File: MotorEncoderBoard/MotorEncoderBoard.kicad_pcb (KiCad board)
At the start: 2 copper layers, 24.3 x 31.8 mm, 13 parts, among them P1 PWR, P2 Out, U1 RPI-579N1, U2 LM311N

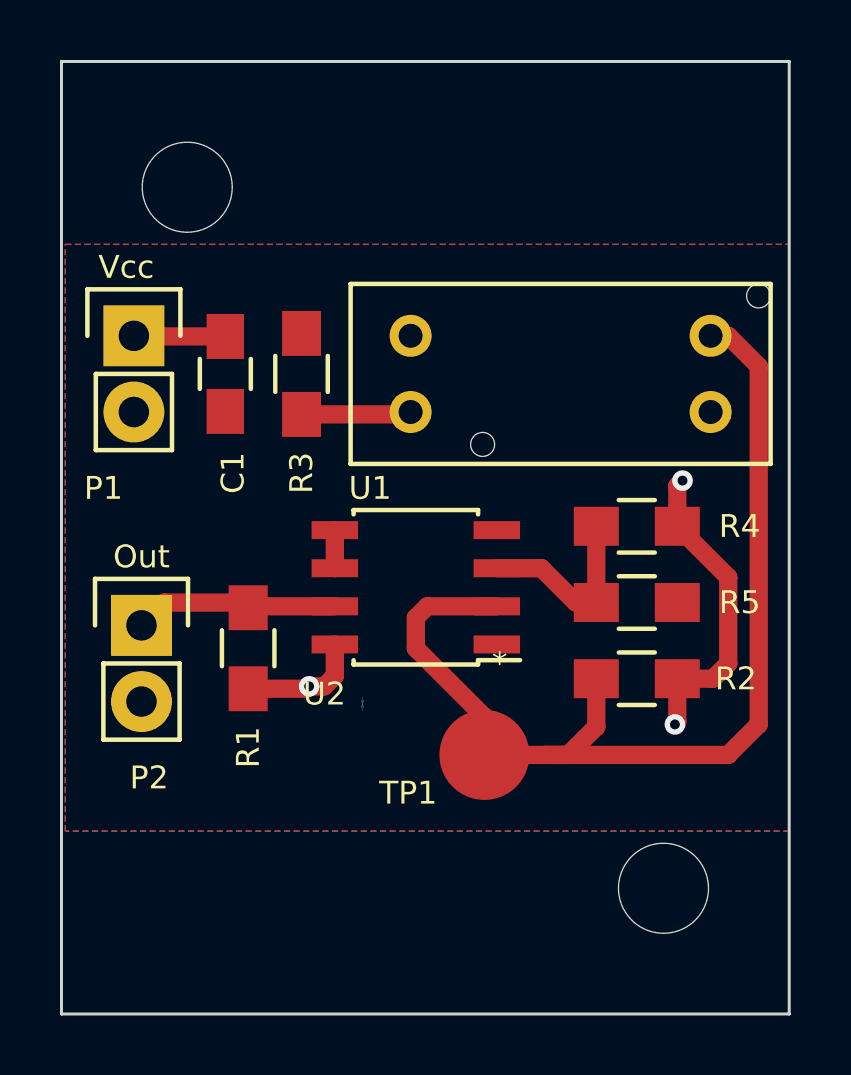
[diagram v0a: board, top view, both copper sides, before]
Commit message: Correction to the motor encoder board
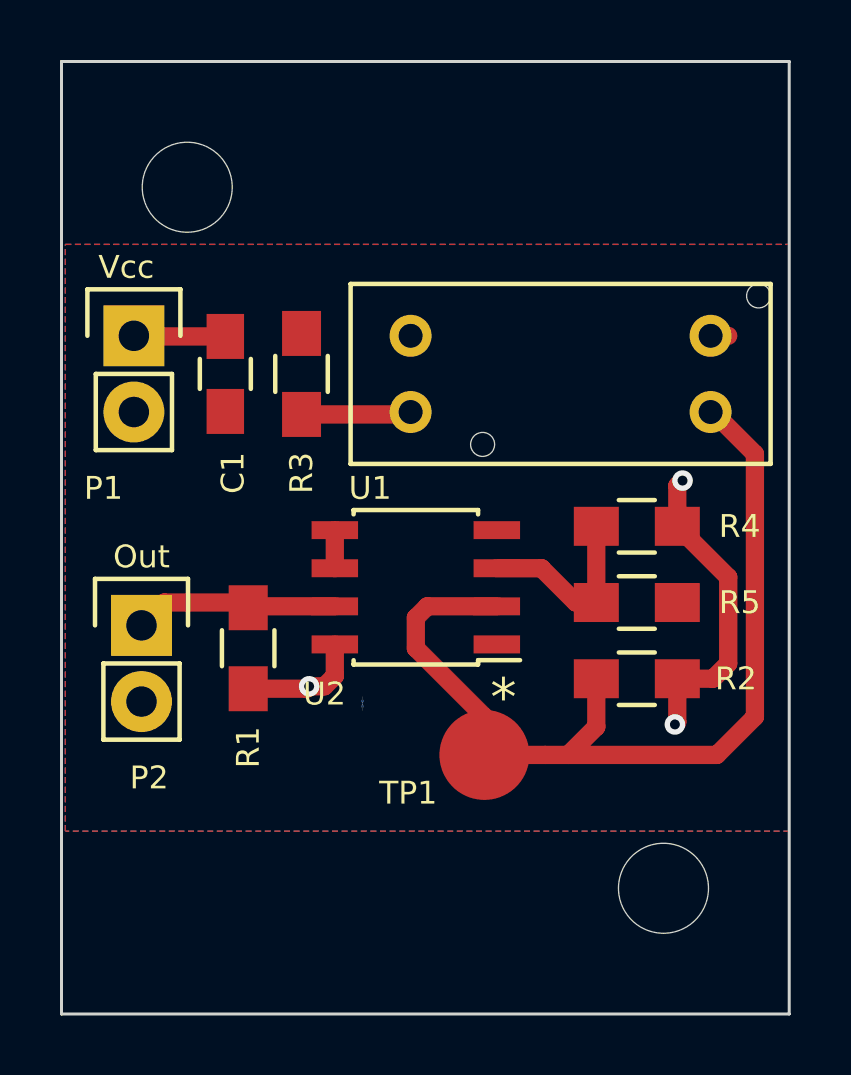
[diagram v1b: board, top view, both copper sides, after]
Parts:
- C1: value C -> 10u
- U2: value LM311N -> LM311D
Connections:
- U1 pad 3: GND -> /OptoOut
- U1 pad 4: /OptoOut -> GND
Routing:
- net /OptoOut: track 35.9 -> 31.7 mm
- net GND: track 0.00 -> 0.92 mm
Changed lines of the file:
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@@
-(kicad_pcb (version 4) (host pcbnew 0.201506222247+5806~23~ubuntu14.04.1-product)
+(kicad_pcb (version 4) (host pcbnew no-vcs-found-product)
   (general
     (links 22)
     (no_connects 0)
-    (area 144.971679 75.34104 176.206241 111.40216)
+    (area 148.412999 77.165999 172.770001 109.016001)
     (thickness 1.6)
     (drawings 16)
-    (tracks 44)
+    (tracks 45)
     (zones 0)
     (modules 13)
@@
       (effects (font (size 0.762 0.762) (thickness 0.127)))
     )
-    (fp_text value C (at 0 2.1 270) (layer F.Fab)
+    (fp_text value 10u (at 0 2.1 270) (layer F.Fab)
       (effects (font (size 0.762 0.762) (thickness 0.127)))
     )
@@
     (pad "" np_thru_hole circle (at 2.6 -2.35 180) (size 0.8 0.8) (drill 0.8) (layers *.Cu *.Mask F.SilkS))
     (pad 3 thru_hole circle (at -5 -1.27 180) (size 1.4 1.4) (drill 0.8) (layers *.Cu *.Mask F.SilkS)
-      (net 2 GND))
+      (net 4 /OptoOut))
     (pad 4 thru_hole circle (at -5 1.27 180) (size 1.4 1.4) (drill 0.8) (layers *.Cu *.Mask F.SilkS)
-      (net 4 /OptoOut))
+      (net 2 GND))
     (pad 2 thru_hole circle (at 5 -1.27 180) (size 1.4 1.4) (drill 0.8) (layers *.Cu *.Mask F.SilkS)
       (net 5 "Net-(R3-Pad1)"))
@@
       (effects (font (size 0.762 0.762) (thickness 0.127)))
     )
-    (fp_text value LM311N (at 0 3.5 180) (layer F.Fab)
+    (fp_text value LM311D (at 0 3.5 180) (layer F.Fab)
       (effects (font (size 0.762 0.762) (thickness 0.127)))
     )
@@
     (effects (font (size 0.762 0.762) (thickness 0.127)))
   )
-  (gr_text * (at 163.068 97.282) (layer F.SilkS)
-    (effects (font (size 0.762 0.762) (thickness 0.127)) (justify mirror))
+  (gr_text * (at 163.195 98.425) (layer F.SilkS)
+    (effects (font (size 1.27 1.27) (thickness 0.127)) (justify mirror))
   )
   (gr_text * (at 158.496 98.806) (layer B.Cu)
@@
   (segment (start 157.574 97.696) (end 157.574 96.647) (width 0.6096) (layer F.Cu) (net 1))
   (segment (start 157.226 98.044) (end 157.574 97.696) (width 0.6096) (layer F.Cu) (net 1))
+  (segment (start 170.1 86.36) (end 170.688 86.36) (width 0.6096) (layer F.Cu) (net 2))
+  (segment (start 170.1 86.36) (end 170.434 86.36) (width 0.6096) (layer F.Cu) (net 2))
   (segment (start 157.574 95.377) (end 154.733 95.377) (width 0.6096) (layer F.Cu) (net 3))
   (segment (start 154.733 95.377) (end 154.606 95.25) (width 0.6096) (layer F.Cu) (net 3))
   (segment (start 154.606 95.25) (end 151.892 95.25) (width 0.6096) (layer F.Cu) (net 3))
   (segment (start 151.892 95.25) (end 151.13 96.012) (width 0.6096) (layer F.Cu) (net 3))
-  (segment (start 170.1 86.36) (end 170.688 86.36) (width 0.6096) (layer F.Cu) (net 4))
-  (segment (start 170.688 86.36) (end 171.704 87.376) (width 0.6096) (layer F.Cu) (net 4))
-  (segment (start 170.688 100.33) (end 164.592 100.33) (width 0.6096) (layer F.Cu) (net 4))
-  (segment (start 171.704 99.314) (end 170.688 100.33) (width 0.6096) (layer F.Cu) (net 4))
-  (segment (start 171.704 87.376) (end 171.704 99.314) (width 0.6096) (layer F.Cu) (net 4))
-  (segment (start 170.1 86.36) (end 170.434 86.36) (width 0.6096) (layer F.Cu) (net 4))
+  (segment (start 170.1 88.9) (end 170.18 88.9) (width 0.6096) (layer F.Cu) (net 4) (status C00000))
+  (segment (start 170.18 88.9) (end 171.577 90.297) (width 0.6096) (layer F.Cu) (net 4) (status 400000))
+  (segment (start 171.577 90.297) (end 171.577 99.06) (width 0.6096) (layer F.Cu) (net 4))
+  (segment (start 171.577 99.06) (end 170.307 100.33) (width 0.6096) (layer F.Cu) (net 4))
+  (segment (start 170.307 100.33) (end 165.354 100.33) (width 0.6096) (layer F.Cu) (net 4))
   (segment (start 162.56 100.33) (end 162.56 99.06) (width 0.6096) (layer F.Cu) (net 4))
   (segment (start 162.56 99.06) (end 160.274 96.774) (width 0.6096) (layer F.Cu) (net 4))

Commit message: Regenerated Gerbers for new boards and stensils
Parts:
- TP1: footprint Measurement_Points:Measurement_Point_Round-SMD-Pad_Big -> Pin_Headers:Pin_Header_Straight_1x01
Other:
- board text added: "Motor Encoder 2L.2"
- board text added: "go! Go! GO!"
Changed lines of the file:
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@@
     (links 22)
     (no_connects 0)
-    (area 148.412999 77.165999 172.770001 109.016001)
+    (area 144.971679 75.34104 176.206241 111.40216)
     (thickness 1.6)
-    (drawings 16)
+    (drawings 18)
     (tracks 45)
     (zones 0)
@@
   )
   (setup
-    (last_trace_width 0.6096)
+    (last_trace_width 0.1524)
     (user_trace_width 0.3048)
     (user_trace_width 0.6096)
@@
     (visible_elements FFFEFF7F)
     (pcbplotparams
-      (layerselection 0x0103c_80000001)
+      (layerselection 0x010fc_80000001)
       (usegerberextensions true)
       (excludeedgelayer true)
@@
     )
   )
-  (module Measurement_Points:Measurement_Point_Round-SMD-Pad_Big (layer F.Cu)
-    (at 162.56 100.33)
-    (descr "Mesurement Point, Round, SMD Pad, DM 3mm,")
-    (tags "Mesurement Point, Round, SMD Pad, DM 3mm,")
-    (fp_text reference TP1 (at -2.54 1.27) (layer F.SilkS)
-      (effects (font (size 0.762 0.762) (thickness 0.127)))
-    )
-    (fp_text value OptoOut (at 2.54 3.81) (layer F.Fab)
-      (effects (font (size 0.762 0.762) (thickness 0.127)))
-    )
-    (pad 1 smd circle (at 0 0) (size 2.99974 2.99974) (layers F.Cu F.Paste F.Mask)
-      (net 4 /OptoOut))
-  )
   (module Gogogo-Footprint:RPI-579N1 (layer F.Cu)
     (at 165.1 87.63 180)
@@
     )
     (pad "" np_thru_hole circle (at 0 0) (size 3 3) (drill 3) (layers *.Cu *.Mask F.SilkS))
+  )
+  (module Pin_Headers:Pin_Header_Straight_1x01 (layer F.Cu)
+    (at 162.56 100.33)
+    (descr "Through hole pin header")
+    (tags "pin header")
+    (fp_text reference TP1 (at 0 -5.1) (layer F.SilkS)
+      (effects (font (size 1 1) (thickness 0.15)))
+    )
+    (fp_text value OptoOut (at 0 -3.1) (layer F.Fab)
+      (effects (font (size 1 1) (thickness 0.15)))
+    )
+    (fp_line (start 1.55 -1.55) (end 1.55 0) (layer F.SilkS) (width 0.15))
+    (fp_line (start -1.75 -1.75) (end -1.75 1.75) (layer F.CrtYd) (width 0.05))
+    (fp_line (start 1.75 -1.75) (end 1.75 1.75) (layer F.CrtYd) (width 0.05))
+    (fp_line (start -1.75 -1.75) (end 1.75 -1.75) (layer F.CrtYd) (width 0.05))
+    (fp_line (start -1.75 1.75) (end 1.75 1.75) (layer F.CrtYd) (width 0.05))
+    (fp_line (start -1.55 0) (end -1.55 -1.55) (layer F.SilkS) (width 0.15))
+    (fp_line (start -1.55 -1.55) (end 1.55 -1.55) (layer F.SilkS) (width 0.15))
+    (fp_line (start -1.27 1.27) (end 1.27 1.27) (layer F.SilkS) (width 0.15))
+    (pad 1 thru_hole rect (at 0 0) (size 2.2352 2.2352) (drill 1.016) (layers *.Cu *.Mask F.SilkS)
+      (net 4 /OptoOut))
+    (model Pin_Headers.3dshapes/Pin_Header_Straight_1x01.wrl
+      (at (xyz 0 0 0))
+      (scale (xyz 1 1 1))
+      (rotate (xyz 0 0 90))
+    )
+  )
+  (gr_text "go! Go! GO!" (at 149.352 104.775) (layer F.SilkS)
+    (effects (font (size 0.762 0.762) (thickness 0.127)) (justify left))
+  )
+  (gr_text "Motor Encoder 2L.2" (at 149.225 103.632) (layer F.SilkS)
+    (effects (font (size 0.762 0.762) (thickness 0.127)) (justify left))
   )
   (gr_line (start 148.463 108.966) (end 172.72 108.966) (angle 90) (layer Edge.Cuts) (width 0.1))
@@
   (segment (start 154.606 95.25) (end 151.892 95.25) (width 0.6096) (layer F.Cu) (net 3))
   (segment (start 151.892 95.25) (end 151.13 96.012) (width 0.6096) (layer F.Cu) (net 3))
-  (segment (start 170.1 88.9) (end 170.18 88.9) (width 0.6096) (layer F.Cu) (net 4) (status C00000))
-  (segment (start 170.18 88.9) (end 171.577 90.297) (width 0.6096) (layer F.Cu) (net 4) (status 400000))
+  (segment (start 170.1 88.9) (end 170.18 88.9) (width 0.6096) (layer F.Cu) (net 4))
+  (segment (start 170.18 88.9) (end 171.577 90.297) (width 0.6096) (layer F.Cu) (net 4))
   (segment (start 171.577 90.297) (end 171.577 99.06) (width 0.6096) (layer F.Cu) (net 4))
   (segment (start 171.577 99.06) (end 170.307 100.33) (width 0.6096) (layer F.Cu) (net 4))

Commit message: Final corrections after testing
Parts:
- R2: value 1K -> 10K
- U1: footprint Gogogo-Footprint:RPI-579N1 -> Gogogo-footprints:RPI-579N1
- moved TP1 0.14 mm to (162.6, 100.2)
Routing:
- net GND: track 0.92 -> 0.00 mm
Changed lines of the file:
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@@
     (links 22)
     (no_connects 0)
-    (area 144.971679 75.34104 176.206241 111.40216)
+    (area 148.412999 77.165999 172.770001 109.016001)
     (thickness 1.6)
-    (drawings 18)
-    (tracks 45)
+    (drawings 17)
+    (tracks 43)
     (zones 0)
     (modules 13)
@@
     (pad_to_mask_clearance 0)
     (aux_axis_origin 0 0)
-    (visible_elements FFFEFF7F)
+    (visible_elements FFFFFF7F)
     (pcbplotparams
       (layerselection 0x010fc_80000001)
@@
       (effects (font (size 0.762 0.762) (thickness 0.127)))
     )
-    (fp_text value 10u (at 0 2.1 270) (layer F.Fab)
+    (fp_text value 10u (at -0.03 0.224 270) (layer F.Fab)
       (effects (font (size 0.762 0.762) (thickness 0.127)))
     )
@@
       (effects (font (size 0.762 0.762) (thickness 0.127)))
     )
-    (fp_text value PWR (at 0 -3.1) (layer F.Fab)
+    (fp_text value PWR (at 0.024 -2.46) (layer F.Fab)
       (effects (font (size 0.762 0.762) (thickness 0.127)))
     )
@@
       (effects (font (size 0.762 0.762) (thickness 0.127)))
     )
-    (fp_text value Out (at 0 -3.1) (layer F.Fab)
+    (fp_text value Out (at 0.07 -2.212) (layer F.Fab)
       (effects (font (size 0.762 0.762) (thickness 0.127)))
     )
@@
       (effects (font (size 0.762 0.762) (thickness 0.127)))
     )
-    (fp_text value 1K (at 0 2.1 90) (layer F.Fab)
+    (fp_text value 1K (at -0.226 0.014 90) (layer F.Fab)
       (effects (font (size 0.762 0.762) (thickness 0.127)))
     )
@@
       (effects (font (size 0.762 0.762) (thickness 0.127)))
     )
-    (fp_text value 1K (at 0 2.1 180) (layer F.Fab)
+    (fp_text value 10K (at -0.16 -0.21 180) (layer F.Fab)
       (effects (font (size 0.762 0.762) (thickness 0.127)))
     )
@@
       (effects (font (size 0.762 0.762) (thickness 0.127)))
     )
-    (fp_text value 100 (at 0 2.1 90) (layer F.Fab)
+    (fp_text value 100 (at -0.07 0.036 90) (layer F.Fab)
       (effects (font (size 0.762 0.762) (thickness 0.127)))
     )
@@
       (effects (font (size 0.762 0.762) (thickness 0.127)))
     )
-    (fp_text value 1K (at 0 2.1 180) (layer F.Fab)
+    (fp_text value 1K (at -0.16 0.01 180) (layer F.Fab)
       (effects (font (size 0.762 0.762) (thickness 0.127)))
     )
@@
       (effects (font (size 0.762 0.762) (thickness 0.127)))
     )
-    (fp_text value 1K (at 0 2.1) (layer F.Fab)
+    (fp_text value 1K (at 0.06 0.05) (layer F.Fab)
       (effects (font (size 0.762 0.762) (thickness 0.127)))
     )
@@
     )
   )
-  (module Gogogo-Footprint:RPI-579N1 (layer F.Cu)
-    (at 165.1 87.63 180)
-    (fp_text reference U1 (at 6.35 -3.81 180) (layer F.SilkS)
-      (effects (font (size 0.762 0.762) (thickness 0.127)))
-    )
-    (fp_text value RPI-579N1 (at -0.07874 -3.8862 180) (layer F.Fab)
-      (effects (font (size 0.762 0.762) (thickness 0.127)))
-    )
-    (fp_line (start -7 -3) (end 7 -3) (layer F.SilkS) (width 0.15))
-    (fp_line (start 7 -3) (end 7 3) (layer F.SilkS) (width 0.15))
-    (fp_line (start 7 3) (end -7 3) (layer F.SilkS) (width 0.15))
-    (fp_line (start -7 3) (end -7 -3) (layer F.SilkS) (width 0.15))
-    (pad "" np_thru_hole circle (at -6.6 2.6 180) (size 0.8 0.8) (drill 0.8) (layers *.Cu *.Mask F.SilkS))
-    (pad "" np_thru_hole circle (at 2.6 -2.35 180) (size 0.8 0.8) (drill 0.8) (layers *.Cu *.Mask F.SilkS))
-    (pad 3 thru_hole circle (at -5 -1.27 180) (size 1.4 1.4) (drill 0.8) (layers *.Cu *.Mask F.SilkS)
-      (net 4 /OptoOut))
-    (pad 4 thru_hole circle (at -5 1.27 180) (size 1.4 1.4) (drill 0.8) (layers *.Cu *.Mask F.SilkS)
-      (net 2 GND))
-    (pad 2 thru_hole circle (at 5 -1.27 180) (size 1.4 1.4) (drill 0.8) (layers *.Cu *.Mask F.SilkS)
-      (net 5 "Net-(R3-Pad1)"))
-    (pad 1 thru_hole circle (at 5 1.27 180) (size 1.4 1.4) (drill 0.8) (layers *.Cu *.Mask F.SilkS)
-      (net 1 VCC))
-  )
   (module Housings_SOIC:SOIC-8_3.9x4.9mm_Pitch1.27mm (layer F.Cu)
     (at 160.274 94.742 180)
@@
       (effects (font (size 0.762 0.762) (thickness 0.127)))
     )
-    (fp_text value LM311D (at 0 3.5 180) (layer F.Fab)
+    (fp_text value LM311D (at -0.126 0.042 270) (layer F.Fab)
       (effects (font (size 0.762 0.762) (thickness 0.127)))
     )
@@
   )
   (module Pin_Headers:Pin_Header_Straight_1x01 (layer F.Cu)
-    (at 162.56 100.33)
+    (at 162.6 100.2)
     (descr "Through hole pin header")
     (tags "pin header")
-    (fp_text reference TP1 (at 0 -5.1) (layer F.SilkS)
-      (effects (font (size 1 1) (thickness 0.15)))
-    )
-    (fp_text value OptoOut (at 0 -3.1) (layer F.Fab)
+    (fp_text reference TP1 (at -3.2 0) (layer F.SilkS)
+      (effects (font (size 1 1) (thickness 0.15)))
+    )
+    (fp_text value OptoOut (at 0 1.9) (layer F.Fab)
       (effects (font (size 1 1) (thickness 0.15)))
     )
@@
       (rotate (xyz 0 0 90))
     )
+  )
+  (module Gogogo-footprints:RPI-579N1 (layer F.Cu)
+    (at 165.1 87.63 180)
+    (fp_text reference U1 (at -0.00254 3.99288 180) (layer F.SilkS)
+      (effects (font (size 1 1) (thickness 0.15)))
+    )
+    (fp_text value RPI-579N1 (at -0.3 -0.07 180) (layer F.Fab)
+      (effects (font (size 1 1) (thickness 0.15)))
+    )
+    (fp_line (start -7 -3) (end 7 -3) (layer F.SilkS) (width 0.15))
+    (fp_line (start 7 -3) (end 7 3) (layer F.SilkS) (width 0.15))
+    (fp_line (start 7 3) (end -7 3) (layer F.SilkS) (width 0.15))
+    (fp_line (start -7 3) (end -7 -3) (layer F.SilkS) (width 0.15))
+    (pad "" np_thru_hole circle (at -6.6 2.6 180) (size 0.8 0.8) (drill 0.8) (layers *.Cu *.Mask F.SilkS))
+    (pad "" np_thru_hole circle (at 2.6 -2.35 180) (size 0.8 0.8) (drill 0.8) (layers *.Cu *.Mask F.SilkS))
+    (pad 3 thru_hole circle (at -5 -1.27 180) (size 1.4 1.4) (drill 0.8) (layers *.Cu *.Mask F.SilkS)
+      (net 4 /OptoOut))
+    (pad 4 thru_hole circle (at -5 1.27 180) (size 1.4 1.4) (drill 0.8) (layers *.Cu *.Mask F.SilkS)
+      (net 2 GND))
+    (pad 2 thru_hole circle (at 5 -1.27 180) (size 1.4 1.4) (drill 0.8) (layers *.Cu *.Mask F.SilkS)
+      (net 5 "Net-(R3-Pad1)"))
+    (pad 1 thru_hole circle (at 5 1.27 180) (size 1.4 1.4) (drill 0.8) (layers *.Cu *.Mask F.SilkS)
+      (net 1 VCC))
   )
   (gr_text "go! Go! GO!" (at 149.352 104.775) (layer F.SilkS)
@@
   (gr_text * (at 163.195 98.425) (layer F.SilkS)
     (effects (font (size 1.27 1.27) (thickness 0.127)) (justify mirror))
-  )
-  (gr_text * (at 158.496 98.806) (layer B.Cu)
-    (effects (font (size 0.762 0.127) (thickness 0.03175)) (justify mirror))
   )
   (segment (start 153.924 86.38) (end 150.896 86.38) (width 0.6096) (layer F.Cu) (net 1))
@@
   (segment (start 157.574 97.696) (end 157.574 96.647) (width 0.6096) (layer F.Cu) (net 1))
   (segment (start 157.226 98.044) (end 157.574 97.696) (width 0.6096) (layer F.Cu) (net 1))
-  (segment (start 170.1 86.36) (end 170.688 86.36) (width 0.6096) (layer F.Cu) (net 2))
-  (segment (start 170.1 86.36) (end 170.434 86.36) (width 0.6096) (layer F.Cu) (net 2))
   (segment (start 157.574 95.377) (end 154.733 95.377) (width 0.6096) (layer F.Cu) (net 3))
   (segment (start 154.733 95.377) (end 154.606 95.25) (width 0.6096) (layer F.Cu) (net 3))
